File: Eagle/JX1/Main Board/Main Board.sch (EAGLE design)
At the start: 9 parts, among them J1 RASPBERRYPI-40-PIN-GPIO_PTH_N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, U1 SN74HC595N, U2 SN74HC595N

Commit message: More board Changes
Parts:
- removed J1: RASPBERRYPI-40-PIN-GPIO_PTH_NO_SHROUD, SparkFun-Connectors:RASPBERRYPI-40-PIN-GPIO_PTH_NO_SHROUD
- added POWER_CONN, SERIAL_CONN: (no value), pinhead:PINHD-1X3
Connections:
- net N$19 renamed SCK
- net N$20 renamed MOSI
- net N$21 renamed MISO
- net N$23 renamed SSCK
- net N$24 renamed SCL
- net N$25 renamed RCK
- removed net N$26: J1.RXI, MODUL1.D1/TX
- new net N$1: MODUL1.D1/TX, SERIAL_CONN.2
- net +5V: now also POWER_CONN.2; no longer J1.5V@2, J1.5V@4
- net GND: now also POWER_CONN.1, POWER_CONN.3; no longer J1.GND@39
- net N$27: now also SERIAL_CONN.1, SERIAL_CONN.3; no longer J1.TXO
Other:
- moved on the sheet: B1, B2, B3, B4, MODUL1, POWER, U1, U2

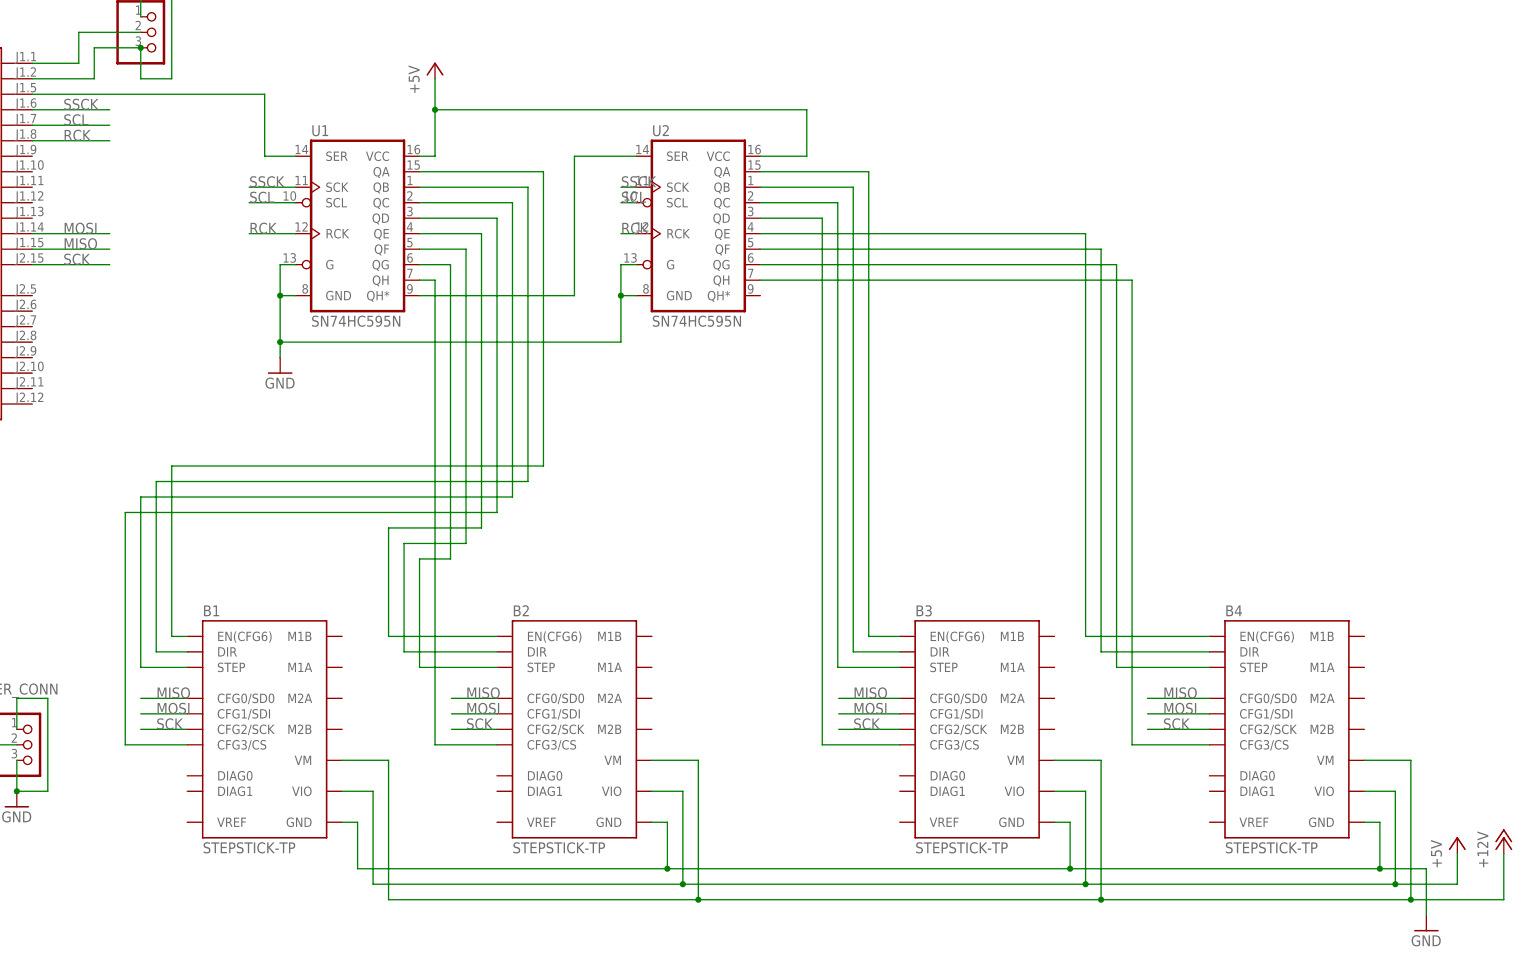
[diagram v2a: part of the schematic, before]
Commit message: Hand-routing the board
Made changes to pin connections for better, neater routing.
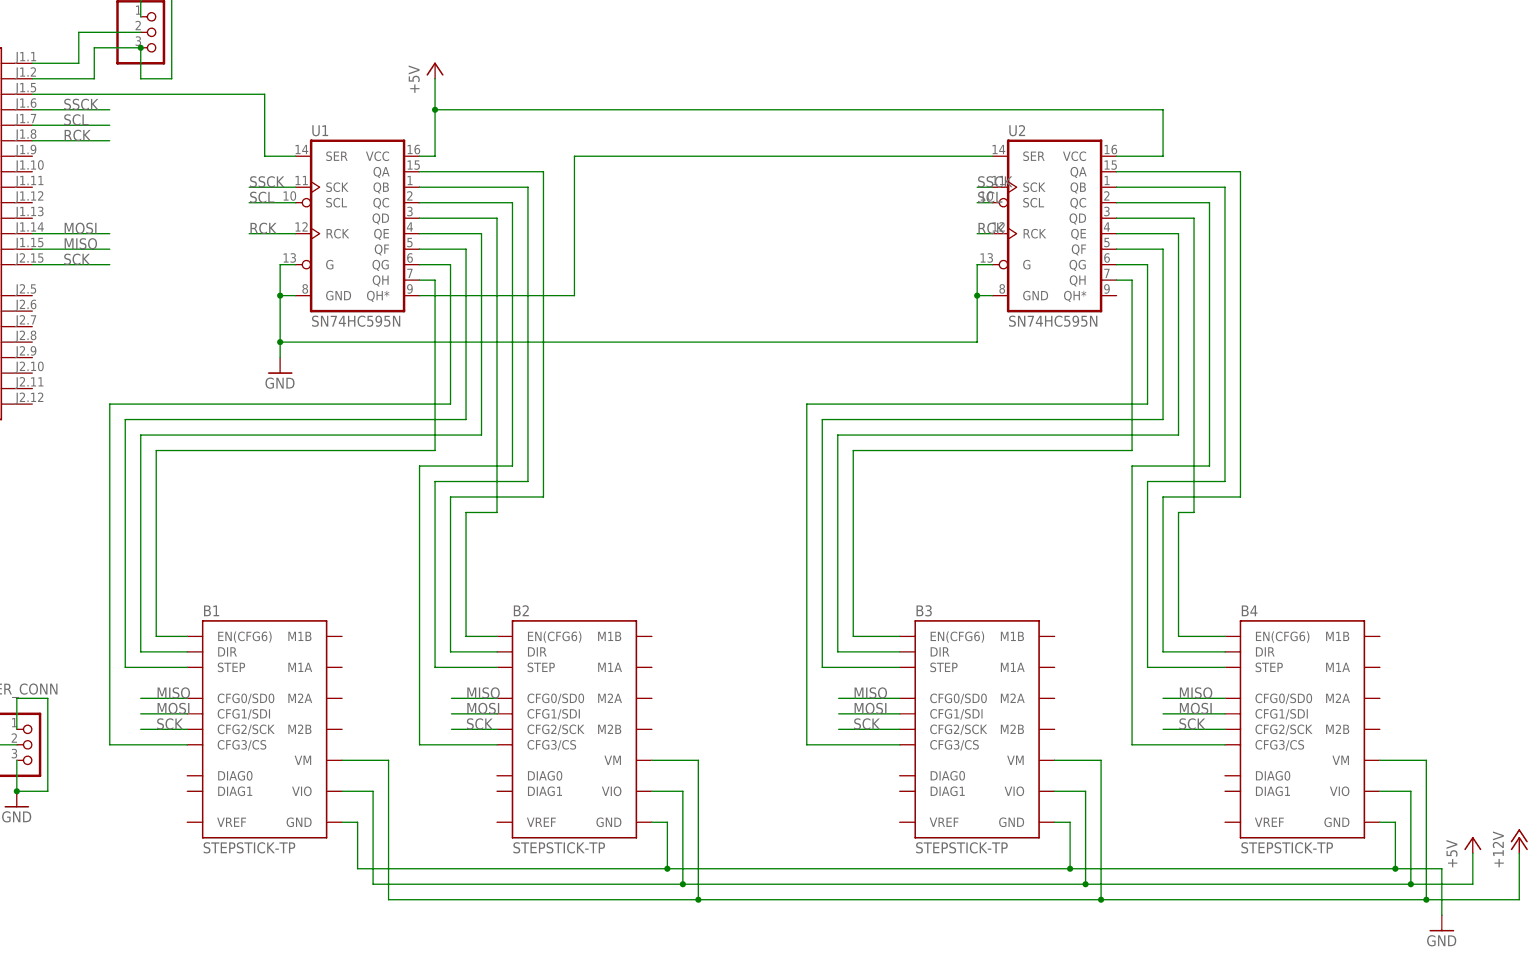
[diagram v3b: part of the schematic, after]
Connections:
- removed net N$10: B1.EN(CFG6), U1.QA
- removed net N$12: B4.STEP, U2.QG
- removed net N$14: B4.EN(CFG6), U2.QE
- removed net N$17: B3.DIR, U2.QB
- removed net N$4: B2.STEP, U1.QG
- removed net N$5: B2.DIR, U1.QF
- removed net N$6: B2.EN(CFG6), U1.QE
- removed net N$7: B1.CFG3/CS, U1.QD
- removed net N$8: B1.STEP, U1.QC
- removed net N$9: B1.DIR, U1.QB
- new net N$20: B1.DIR, U1.QE
- new net N$21: B1.STEP, U1.QF
- new net N$23: B1.CFG3/CS, U1.QG
- new net N$24: B2.STEP, U1.QB
- new net N$25: B2.DIR, U1.QA
- new net N$26: B2.EN(CFG6), U1.QD
- new net N$28: B1.EN(CFG6), U1.QH
- new net N$30: B3.DIR, U2.QE
- new net N$33: B4.EN(CFG6), U2.QD
- new net N$35: B4.STEP, U2.QB
- net N$11: now also B3.EN(CFG6); no longer B4.CFG3/CS
- net N$13: now also B3.STEP; no longer B4.DIR
- net N$15: now also U2.QG; no longer U2.QD
- net N$16: now also B4.CFG3/CS; no longer B3.STEP
- net N$18: now also B4.DIR; no longer B3.EN(CFG6)
- net N$3: now also U1.QC; no longer U1.QH
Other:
- moved on the sheet: B4, U2

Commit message: Routed Main Board
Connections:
- new net NC: MODUL1.+5V
- net N$22: now also MODUL1.D5; no longer MODUL1.D2
- net RCK: now also MODUL1.D7; no longer MODUL1.D5
- net SCL: now also MODUL1.D9; no longer MODUL1.D4
- net SSCK: now also MODUL1.D8; no longer MODUL1.D3
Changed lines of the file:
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@@
 </variantdefs>
 <classes>
-<class number="0" name="default" width="0" drill="0">
+<class number="0" name="default" width="0.254" drill="0">
 </class>
 <class number="1" name="Data" width="0.0254" drill="0">
@@
 <net name="N$22" class="1">
 <segment>
-<pinref part="MODUL1" gate="MODUL" pin="D2"/>
-<wire x1="73.66" y1="147.32" x2="111.76" y2="147.32" width="0.1524" layer="91"/>
-<wire x1="111.76" y1="147.32" x2="111.76" y2="137.16" width="0.1524" layer="91"/>
 <pinref part="U1" gate="U1" pin="SER"/>
-<wire x1="111.76" y1="137.16" x2="116.84" y2="137.16" width="0.1524" layer="91"/>
+<wire x1="114.3" y1="137.16" x2="116.84" y2="137.16" width="0.1524" layer="91"/>
+<pinref part="MODUL1" gate="MODUL" pin="D5"/>
+<wire x1="73.66" y1="139.7" x2="114.3" y2="139.7" width="0.1524" layer="91"/>
+<wire x1="114.3" y1="139.7" x2="114.3" y2="137.16" width="0.1524" layer="91"/>
 </segment>
 </net>
@@
 <segment>
 <pinref part="U2" gate="U1" pin="SCL"/>
-<wire x1="231.14" y1="129.54" x2="228.6" y2="129.54" width="0.1524" layer="91"/>
-<label x="228.6" y="129.54" size="1.778" layer="95"/>
+<wire x1="231.14" y1="129.54" x2="223.52" y2="129.54" width="0.1524" layer="91"/>
+<label x="223.52" y="129.54" size="1.778" layer="95"/>
 </segment>
 <segment>
@@
 </segment>
 <segment>
-<pinref part="MODUL1" gate="MODUL" pin="D4"/>
-<wire x1="86.36" y1="142.24" x2="73.66" y2="142.24" width="0.1524" layer="91"/>
-<label x="78.74" y="142.24" size="1.778" layer="95"/>
+<pinref part="MODUL1" gate="MODUL" pin="D9"/>
+<wire x1="73.66" y1="129.54" x2="86.36" y2="129.54" width="0.1524" layer="91"/>
+<label x="78.74" y="129.54" size="1.778" layer="95"/>
 </segment>
 </net>
@@
 <segment>
 <pinref part="U2" gate="U1" pin="RCK"/>
-<wire x1="231.14" y1="124.46" x2="228.6" y2="124.46" width="0.1524" layer="91"/>
-<label x="228.6" y="124.46" size="1.778" layer="95"/>
+<wire x1="231.14" y1="124.46" x2="223.52" y2="124.46" width="0.1524" layer="91"/>
+<label x="223.52" y="124.46" size="1.778" layer="95"/>
 </segment>
 <segment>
@@
 </segment>
 <segment>
-<pinref part="MODUL1" gate="MODUL" pin="D5"/>
-<wire x1="86.36" y1="139.7" x2="73.66" y2="139.7" width="0.1524" layer="91"/>
-<label x="78.74" y="139.7" size="1.778" layer="95"/>
+<pinref part="MODUL1" gate="MODUL" pin="D7"/>
+<wire x1="73.66" y1="134.62" x2="86.36" y2="134.62" width="0.1524" layer="91"/>
+<label x="78.74" y="134.62" size="1.778" layer="95"/>
 </segment>
 </net>
 <net name="SSCK" class="0">
-<segment>
-<pinref part="MODUL1" gate="MODUL" pin="D3"/>
-<wire x1="73.66" y1="144.78" x2="86.36" y2="144.78" width="0.1524" layer="91"/>
-<label x="78.74" y="144.78" size="1.778" layer="95"/>
-</segment>
 <segment>
 <pinref part="U1" gate="U1" pin="SCK"/>
@@
 <segment>
 <pinref part="U2" gate="U1" pin="SCK"/>
-<wire x1="231.14" y1="132.08" x2="228.6" y2="132.08" width="0.1524" layer="91"/>
-<label x="228.6" y="132.08" size="1.778" layer="95"/>
+<wire x1="231.14" y1="132.08" x2="223.52" y2="132.08" width="0.1524" layer="91"/>
+<label x="223.52" y="132.08" size="1.778" layer="95"/>
+</segment>
+<segment>
+<pinref part="MODUL1" gate="MODUL" pin="D8"/>
+<wire x1="73.66" y1="132.08" x2="86.36" y2="132.08" width="0.1524" layer="91"/>
+<label x="78.74" y="132.08" size="1.778" layer="95"/>
 </segment>
 </net>
@@
 </segment>
 </net>
-<net name="N$28" class="0">
+<net name="N$28" class="1">
 <segment>
 <pinref part="U1" gate="U1" pin="QH"/>
@@
 </segment>
 </net>
+<net name="NC" class="0">
+<segment>
+<pinref part="MODUL1" gate="MODUL" pin="+5V"/>
+<wire x1="43.18" y1="160.02" x2="43.18" y2="162.56" width="0.1524" layer="91"/>
+<label x="43.18" y="162.56" size="1.778" layer="95"/>
+</segment>
+</net>

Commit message: Started moving traces to make room for thermal stuff
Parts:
- added X1, X2: (no value), con-wago-500:W237-102
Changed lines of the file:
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@@
 <part name="P+5" library="supply1" library_urn="urn:adsk.eagle:library:371" deviceset="+5V" device=""/>
 <part name="GND4" library="supply1" library_urn="urn:adsk.eagle:library:371" deviceset="GND" device=""/>
+<part name="X1" library="con-wago-500" library_urn="urn:adsk.eagle:library:195" deviceset="W237-102" device="" package3d_urn="urn:adsk.eagle:package:10688/1"/>
+<part name="X2" library="con-wago-500" library_urn="urn:adsk.eagle:library:195" deviceset="W237-102" device="" package3d_urn="urn:adsk.eagle:package:10688/1"/>
 </parts>
 <sheets>
@@
 <attribute name="VALUE" x="68.58" y="27.94" size="1.778" layer="96"/>
 </instance>
+<instance part="X1" gate="-1" x="-7.62" y="83.82" smashed="yes">
+<attribute name="NAME" x="-7.62" y="84.709" size="1.778" layer="95" rot="R180"/>
+</instance>
+<instance part="X1" gate="-2" x="-7.62" y="78.74" smashed="yes">
+<attribute name="VALUE" x="-10.16" y="75.057" size="1.778" layer="96"/>
+<attribute name="NAME" x="-7.62" y="79.629" size="1.778" layer="95" rot="R180"/>
+</instance>
+<instance part="X2" gate="-1" x="-7.62" y="68.58" smashed="yes">
+<attribute name="NAME" x="-7.62" y="69.469" size="1.778" layer="95" rot="R180"/>
+</instance>
+<instance part="X2" gate="-2" x="-7.62" y="63.5" smashed="yes">
+<attribute name="VALUE" x="-10.16" y="59.817" size="1.778" layer="96"/>
+<attribute name="NAME" x="-7.62" y="64.389" size="1.778" layer="95" rot="R180"/>
+</instance>
 </instances>

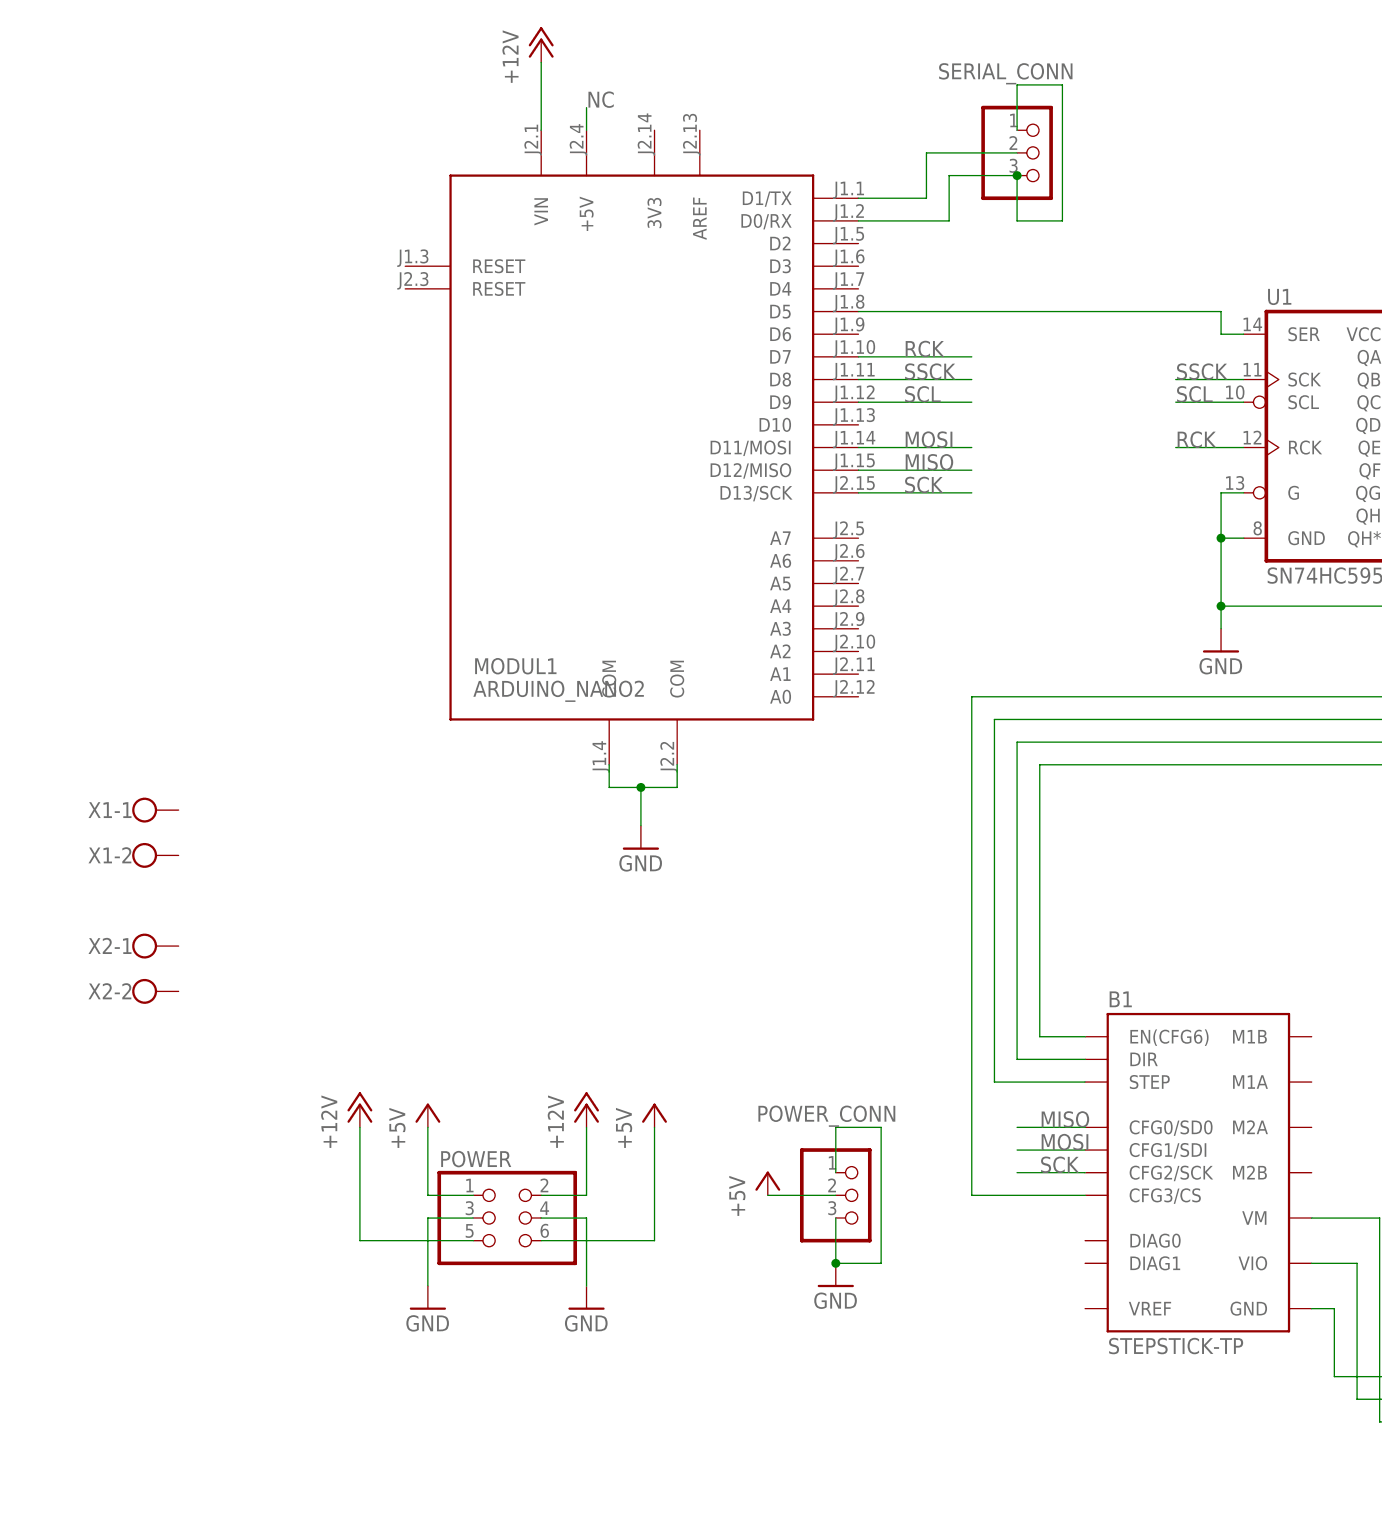
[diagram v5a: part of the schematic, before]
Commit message: Added and connected thermistor terminals
Also added terminals for bed and extruder, but did not connect them.
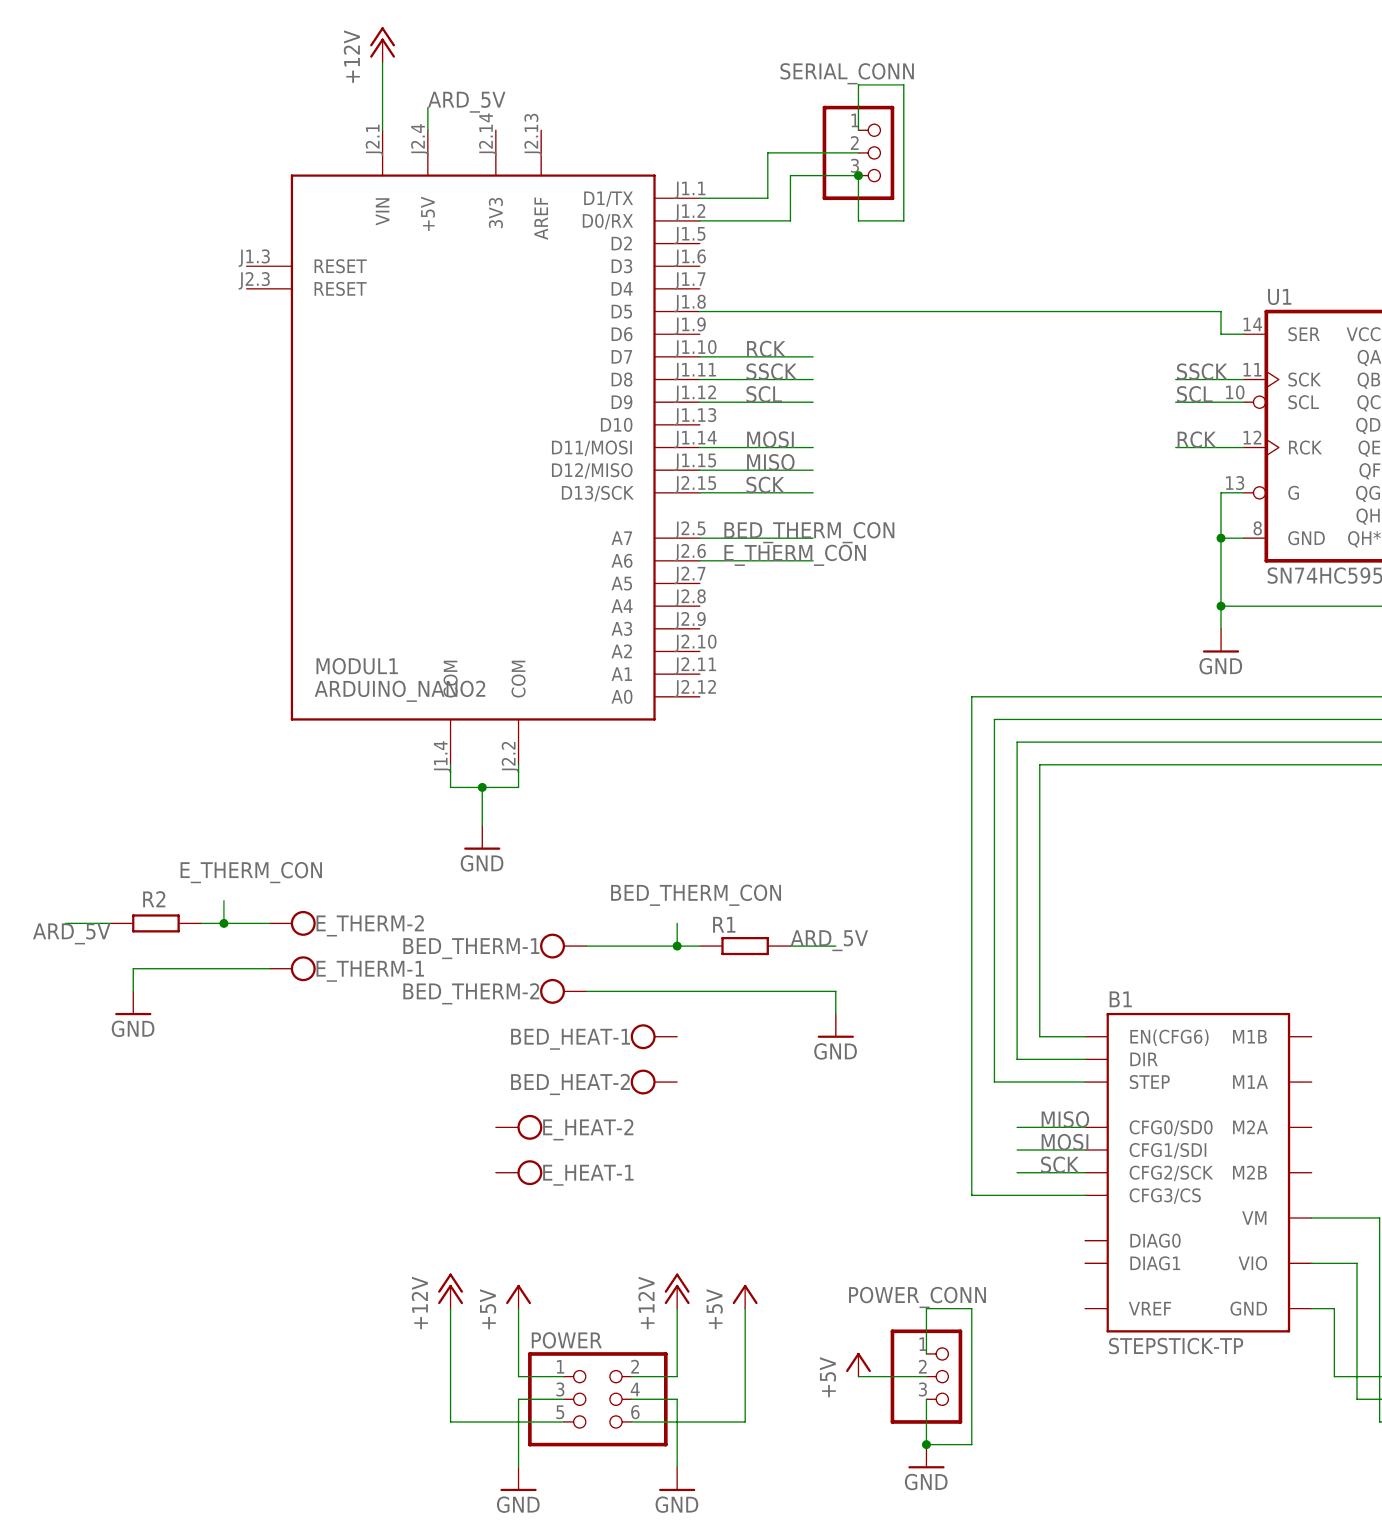
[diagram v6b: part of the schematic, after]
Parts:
- removed X1, X2: (no value), con-wago-500:W237-102
- added BED_HEAT, BED_THERM, E_HEAT, E_THERM: (no value), con-wago-500:W237-102
- added R1, R2: (no value), eagle-ltspice:R0204/7
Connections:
- removed net NC: MODUL1.+5V
- new net ARD_5V: MODUL1.+5V, R1.2, R2.2
- new net BED_THERM_CON: BED_THERM-1.KL, MODUL1.A7, R1.1
- new net E_THERM_CON: E_THERM-2.KL, MODUL1.A6, R2.1
- net GND: now also BED_THERM-2.KL, E_THERM-1.KL
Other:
- moved on the sheet: MODUL1, POWER, POWER_CONN, SERIAL_CONN
